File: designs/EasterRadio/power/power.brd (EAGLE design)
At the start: 31 x 44 mm, 23 parts, among them IC1 MCP73832T-2ACI_OT, IC2 TPS62160DGKR, IC3 DMP1045U-7, J1 10118192-0001LF, J2 S2B-PH-SM4

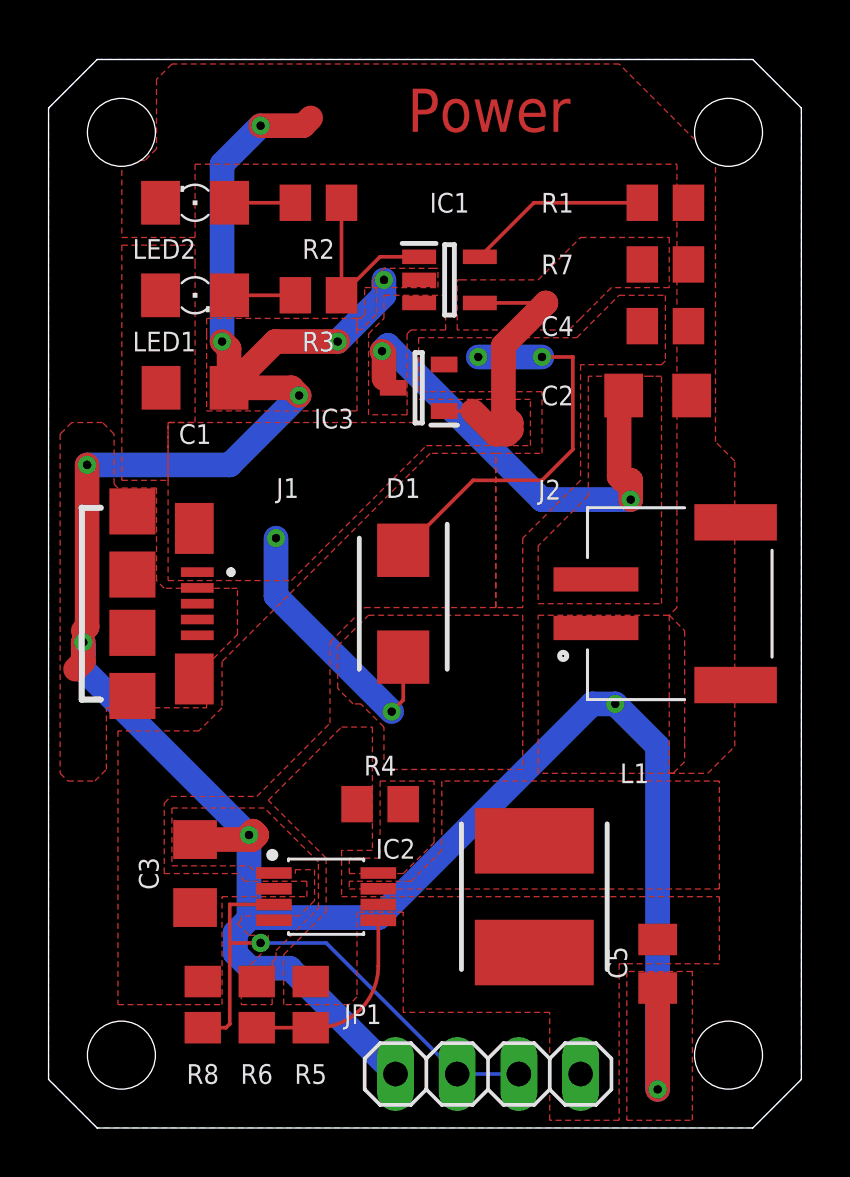
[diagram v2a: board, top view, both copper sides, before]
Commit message: added esd for rs232 to can
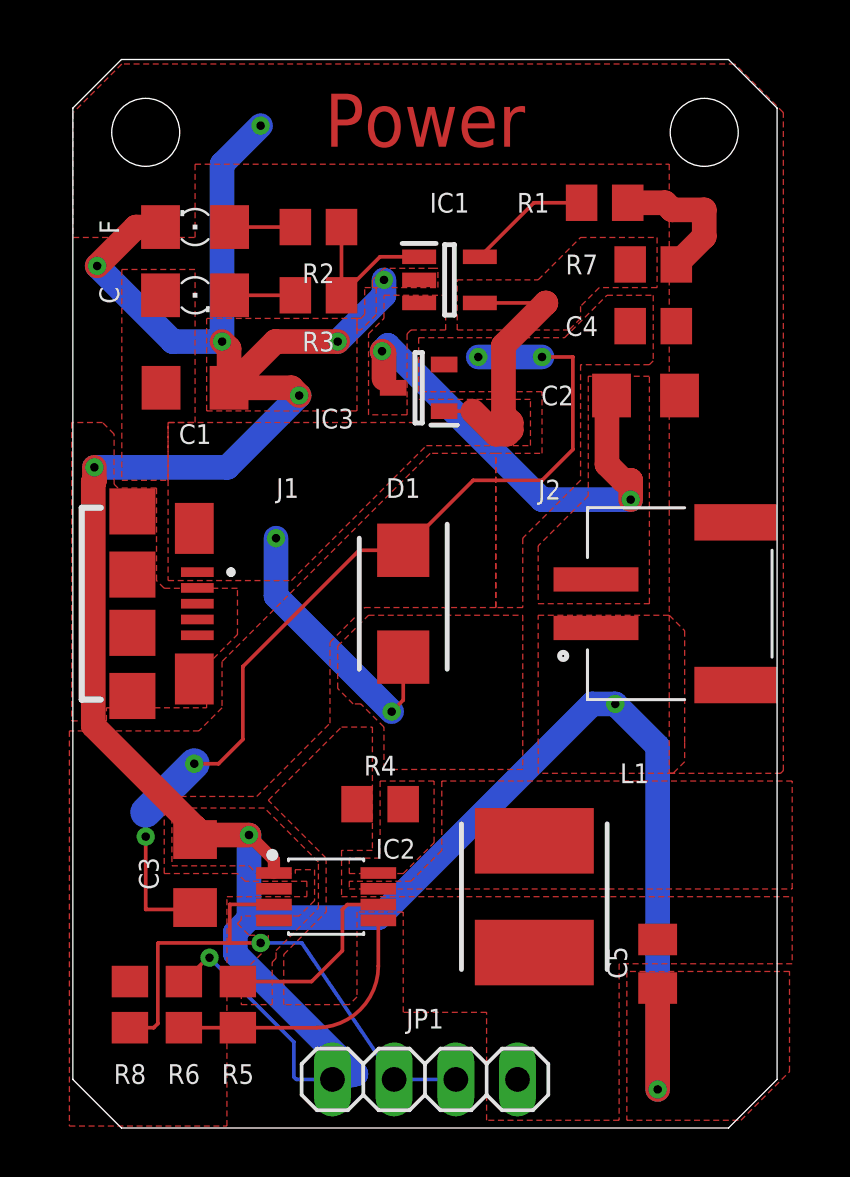
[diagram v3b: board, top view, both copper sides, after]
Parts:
- removed LED2: (no value), CommonParts:1206
- added F: (no value), CommonParts:1206
- moved R5 3.00 mm to (7.79, 5.08)
- moved R6 3.00 mm to (5.57, 5.08)
- moved R8 3.00 mm to (3.35, 5.08)
- moved JP1 2.61 mm to (15.5, 2.00)
- moved R1 2.50 mm to (22.9, 38.1)
- moved R2 1.00 mm to (11.1, 37.1)
- moved C2 0.50 mm to (24.6, 30.2)
- moved C4 0.50 mm to (24.9, 33.0)
- moved R7 0.50 mm to (24.9, 35.6)
- renumbered LED1 to C
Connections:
- net GNDA: now also F.C; no longer LED2.C
- net N$3: now also F.A; no longer LED2.A
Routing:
- net U_DRAIN: track 16.5 -> 39.4 mm, vias 2 -> 4
- net GNDA: track 110.5 -> 132.1 mm, vias 10 -> 11
- net 3.3V: track 0.00 -> 8.09 mm
- net FB: track 7.94 -> 10.9 mm
- net N$1: track 7.61 -> 5.11 mm
- net EN: track 22.1 -> 23.2 mm
- net STAT: track 7.66 -> 6.66 mm
- removed copper zone on layer 16, net GNDA
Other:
- board size 31 x 44 mm -> 29 x 44 mm

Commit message: added mainboard layout and new 3.5mm jack
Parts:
- added D2: LSM115JE3_TR13, CommonParts:DIOM5436X330N
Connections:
- net 5V: now also D2.1, JP1.2
- net EN: no longer JP1.2
- net GNDA: now also D2.2
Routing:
- net 5V: track 23.6 -> 60.7 mm, vias 2 -> 3
- net GNDA: track 132.1 -> 136.8 mm
- net EN: track 23.2 -> 25.0 mm, vias 1 -> 3
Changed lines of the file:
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@@
 <drawing>
 <settings>
-<setting alwaysvectorfont="yes"/>
+<setting alwaysvectorfont="no"/>
 <setting verticaltext="up"/>
 </settings>
-<grid distance="0.5" unitdist="mm" unit="mm" style="lines" multiple="1" display="yes" altdistance="5" altunitdist="mil" altunit="mil"/>
+<grid distance="0.1" unitdist="mm" unit="mm" style="lines" multiple="1" display="yes" altdistance="5" altunitdist="mil" altunit="mil"/>
 <layers>
 <layer number="1" name="Top" color="4" fill="1" visible="yes" active="yes"/>
@@
 <attribute name="VALUE" x="10.42" y="-1.175" size="1.27" layer="27"/>
 </element>
+<element name="D2" library="CommonParts" package="DIOM5436X330N" value="LSM115JE3_TR13" x="15.5" y="6" smashed="yes" rot="MR0">
+<attribute name="DESCRIPTION" value="Schottky Diodes &amp; Rectifiers Schottky" x="15.5" y="6" size="1.778" layer="28" rot="MR0" display="off"/>
+<attribute name="HEIGHT" value="3.3mm" x="15.5" y="6" size="1.778" layer="28" rot="MR0" display="off"/>
+<attribute name="MANUFACTURER_NAME" value="Microsemi Corporation" x="15.5" y="6" size="1.778" layer="28" rot="MR0" display="off"/>
+<attribute name="MANUFACTURER_PART_NUMBER" value="LSM115JE3/TR13" x="15.5" y="6" size="1.778" layer="28" rot="MR0" display="off"/>
+<attribute name="MOUSER_PART_NUMBER" value="494-LSM115JE3/TR13" x="15.5" y="6" size="1.778" layer="28" rot="MR0" display="off"/>
+<attribute name="MOUSER_PRICE-STOCK" value="https://www.mouser.com/Search/Refine.aspx?Keyword=494-LSM115JE3%2FTR13" x="15.5" y="6" size="1.778" layer="28" rot="MR0" display="off"/>
+<attribute name="NAME" x="10.5" y="6" size="0.8128" layer="26" rot="MR0" align="center"/>
+</element>
 </elements>
 <signals>
@@
 <contactref element="IC1" pad="2"/>
 <contactref element="J2" pad="1"/>
-<contactref element="J1" pad="5"/>
 <contactref element="C4" pad="2"/>
 <contactref element="F" pad="C"/>
@@
 <wire x1="9.2804" y1="11.0396" x2="8.255" y2="12.065" width="0.508" layer="1"/>
 <wire x1="5.5725" y1="6.03" x2="6.5557" y2="7.0132" width="0.1524" layer="1"/>
-<wire x1="6.5557" y1="7.0132" x2="6.62781875" y2="7.0132" width="0.1524" layer="1"/>
-<via x="6.62781875" y="7.0132" extent="1-16" drill="0.35"/>
-<wire x1="6.62781875" y1="7.0132" x2="10.1" y2="3.54101875" width="0.1524" layer="16"/>
-<wire x1="10.1" y1="3.54101875" x2="10.1" y2="2.1" width="0.1524" layer="16"/>
+<wire x1="6.5557" y1="7.0132" x2="6.72781875" y2="7.0132" width="0.1524" layer="1"/>
+<via x="6.72781875" y="7.0132" extent="1-16" drill="0.2"/>
+<wire x1="6.72781875" y1="7.0132" x2="10.1" y2="3.64101875" width="0.1524" layer="16"/>
+<wire x1="10.1" y1="3.64101875" x2="10.1" y2="2.1" width="0.1524" layer="16"/>
 <wire x1="10.1" y1="2.1" x2="10.2" y2="2" width="0.1524" layer="16"/>
 <wire x1="10.2" y1="2" x2="11.69" y2="2" width="0.1524" layer="16"/>
@@
 <wire x1="2" y1="35.5" x2="5.115" y2="32.385" width="1.016" layer="16"/>
 <wire x1="5.115" y1="32.385" x2="7.14375" y2="32.385" width="1.016" layer="16"/>
+<contactref element="J1" pad="5"/>
+<contactref element="D2" pad="2"/>
+<wire x1="11.69" y1="2" x2="11.69" y2="4.39" width="1.016" layer="16"/>
+<wire x1="11.69" y1="4.39" x2="13.3" y2="6" width="1.016" layer="16"/>
 </signal>
 <signal name="N$10">
@@
 <vertex x="25.05875" y="34.6075"/>
 <vertex x="22.6775" y="34.6075"/>
-<vertex x="21.9075" y="33.8375"/>
-<vertex x="21.9075" y="33.3375"/>
-<vertex x="21.43125" y="32.86125"/>
+<vertex x="20.93125" y="32.86125"/>
 <vertex x="16.8275" y="32.86125"/>
 </polygon>
@@
 </polygon>
 <wire x1="14.605" y1="19.39" x2="14.605" y2="17.62125" width="0.1524" layer="1"/>
-<wire x1="14.605" y1="17.62125" x2="14.12875" y2="17.145" width="0.1524" layer="1"/>
+<wire x1="14.605" y1="17.62125" x2="14.241875" y2="17.258125" width="0.1524" layer="1"/>
 <via x="14.12875" y="17.145" extent="1-16" drill="0.35"/>
+<wire x1="14.241875" y1="17.258125" x2="14.12875" y2="17.145" width="0.1524" layer="1"/>
 <wire x1="14.12875" y1="17.145" x2="9.36625" y2="21.9075" width="1.016" layer="16"/>
 <wire x1="9.36625" y1="21.9075" x2="9.36625" y2="24.28875" width="1.016" layer="16"/>
@@
 <wire x1="20.47875" y1="33.9725" x2="20.47625" y2="33.975" width="1.016" layer="1"/>
 <wire x1="20.47625" y1="33.975" x2="17.76" y2="33.975" width="0.1524" layer="1"/>
+<contactref element="D2" pad="1"/>
+<contactref element="JP1" pad="2"/>
+<wire x1="17.7" y1="6" x2="16.7" y2="5" width="1.016" layer="16"/>
+<wire x1="16.7" y1="5" x2="15.5" y2="5" width="1.016" layer="16"/>
+<wire x1="15.5" y1="5" x2="14.23" y2="3.73" width="1.016" layer="16"/>
+<wire x1="14.23" y1="3.73" x2="14.23" y2="2" width="1.016" layer="16"/>
+<wire x1="17.7" y1="6" x2="17" y2="6.7" width="1.016" layer="16"/>
+<wire x1="17" y1="6.7" x2="17" y2="9.5" width="1.016" layer="16"/>
+<wire x1="14.741875" y1="17.258125" x2="14.241875" y2="17.258125" width="1.016" layer="1"/>
+<wire x1="14.605" y1="19.39" x2="14.741875" y2="19.253125" width="1.016" layer="1"/>
+<wire x1="14.741875" y1="19.253125" x2="14.741875" y2="17.258125" width="1.016" layer="1"/>
+<wire x1="17" y1="9.5" x2="23.5" y2="9.5" width="1.016" layer="16"/>
+<wire x1="23.5" y1="9.5" x2="23.5" y2="15" width="1.016" layer="16"/>
+<wire x1="23.5" y1="15" x2="23" y2="15" width="1.016" layer="16"/>
+<via x="23" y="15" extent="1-16" drill="0.35"/>
+<wire x1="23" y1="15" x2="19.5" y2="15" width="1.016" layer="1"/>
+<wire x1="18" y1="16.5" x2="18" y2="19.5" width="1.016" layer="1"/>
+<wire x1="18" y1="19.5" x2="14.98875" y2="19.5" width="1.016" layer="1"/>
+<wire x1="14.98875" y1="19.5" x2="14.741875" y2="19.253125" width="1.016" layer="1"/>
+<wire x1="19.5" y1="15" x2="18" y2="16.5" width="1.016" layer="1"/>
 </signal>
 <signal name="U_DRAIN">
@@
 <contactref element="IC2" pad="3"/>
 <contactref element="R8" pad="2"/>
-<contactref element="JP1" pad="2"/>
 <contactref element="JP1" pad="3"/>
 <wire x1="7.46125" y1="7.62" x2="7.46125" y2="9.2075" width="0.1524" layer="1"/>
 <wire x1="7.46125" y1="9.2075" x2="9.2729" y2="9.2075" width="0.1524" layer="1"/>
 <wire x1="9.2729" y1="9.2075" x2="9.2804" y2="9.2" width="0.1524" layer="1"/>
-<wire x1="7.46125" y1="7.62" x2="8.7" y2="7.62" width="0.1524" layer="1"/>
+<wire x1="7.46125" y1="7.62" x2="8.73125" y2="7.62" width="0.1524" layer="1"/>
 <via x="8.73125" y="7.62" extent="1-16" drill="0.3556"/>
-<wire x1="8.7" y1="7.62" x2="8.73125" y2="7.62" width="0.1524" layer="1"/>
-<wire x1="8.73125" y1="7.62" x2="10.43" y2="7.62" width="0.1524" layer="16"/>
-<wire x1="10.43" y1="7.62" x2="14.23" y2="2" width="0.1524" layer="16"/>
-<wire x1="16.77" y1="2" x2="14.23" y2="2" width="0.1524" layer="16"/>
+<wire x1="10.43" y1="7.62" x2="8.73125" y2="7.62" width="0.1524" layer="16"/>
 <wire x1="3.35" y1="4.13" x2="4.33" y2="4.13" width="0.1524" layer="1"/>
 <wire x1="4.33" y1="4.13" x2="4.5" y2="4.3" width="0.1524" layer="1"/>
@@
 <wire x1="4.5" y1="7.6" x2="4.52" y2="7.62" width="0.1524" layer="1"/>
 <wire x1="4.52" y1="7.62" x2="7.46125" y2="7.62" width="0.1524" layer="1"/>
+<wire x1="16.77" y1="2" x2="15.5" y2="3.27" width="0.1524" layer="16"/>
+<wire x1="15.5" y1="3.27" x2="15.5" y2="3.5" width="0.1524" layer="16"/>
+<via x="15.5" y="3.5" extent="1-16" drill="0.35"/>
+<wire x1="15.5" y1="3.5" x2="15.5" y2="7.5" width="0.1524" layer="1"/>
+<via x="15.5" y="7.5" extent="1-16" drill="0.35"/>
+<wire x1="15.5" y1="7.5" x2="10.55" y2="7.5" width="0.1524" layer="16"/>
+<wire x1="10.55" y1="7.5" x2="10.43" y2="7.62" width="0.1524" layer="16"/>
 </signal>
 </signals>

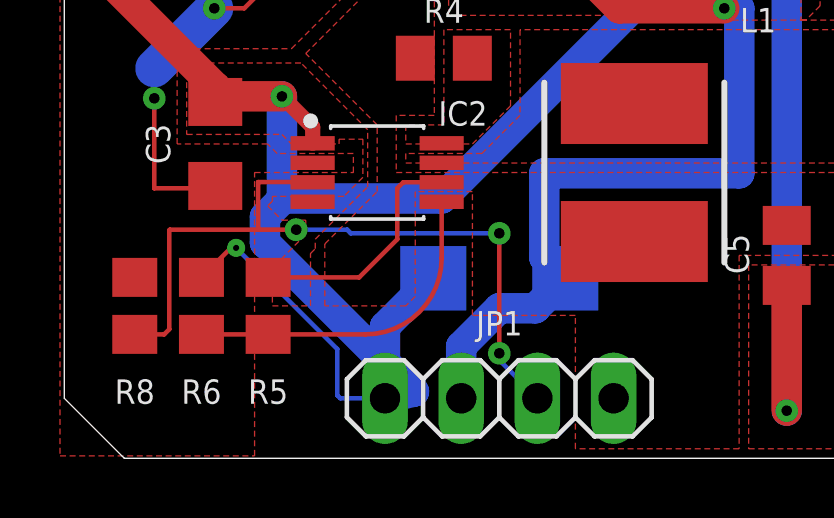
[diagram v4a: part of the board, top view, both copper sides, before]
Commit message: added more stuff to pcb main for radio
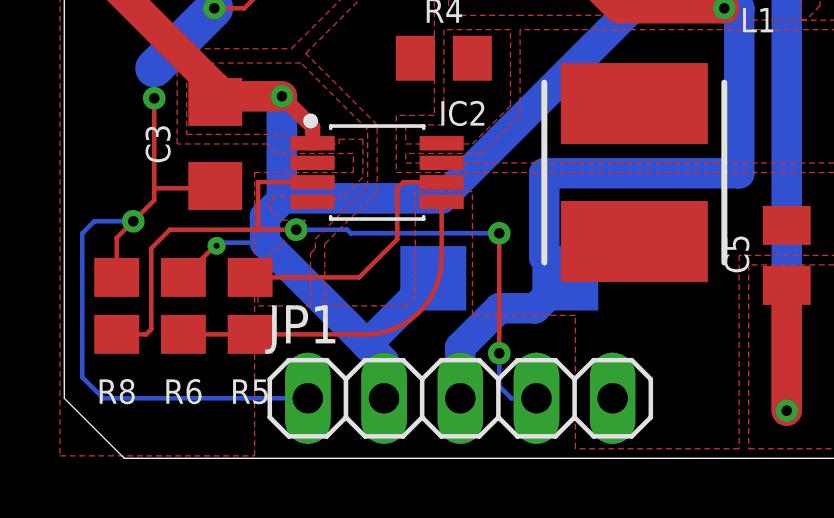
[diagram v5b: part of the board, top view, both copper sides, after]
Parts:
- JP1: device pinhead:1X04 -> pinhead:1X05
- moved JP1 1.30 mm to (14.2, 2.00)
- moved R8 0.60 mm to (2.75, 5.08)
- moved R5 0.60 mm to (7.20, 5.08)
- moved R6 0.60 mm to (4.97, 5.08)
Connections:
- net 3.3V: now also JP1.5; no longer JP1.4
- net 5V: now also JP1.3; no longer JP1.2
- net EN: now also JP1.4; no longer JP1.3
- net GNDA: now also JP1.2; no longer JP1.1
- net U_DRAIN: now also JP1.1
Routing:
- net U_DRAIN: track 39.4 -> 57.4 mm, vias 4 -> 5
- net GNDA: track 136.8 -> 127.9 mm
- net EN: track 25.0 -> 26.0 mm
- net FB: track 10.9 -> 11.5 mm
- net 3.3V: track 8.09 -> 8.69 mm

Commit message: started board routing
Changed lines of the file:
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@@
 <setting verticaltext="up"/>
 </settings>
-<grid distance="0.01" unitdist="mm" unit="mm" style="lines" multiple="1" display="yes" altdistance="5" altunitdist="mil" altunit="mil"/>
+<grid distance="0.1" unitdist="mm" unit="mm" style="lines" multiple="1" display="yes" altdistance="5" altunitdist="mil" altunit="mil"/>
 <layers>
 <layer number="1" name="Top" color="4" fill="1" visible="yes" active="yes"/>
@@
 </element>
 <element name="R5" library="CommonParts" package="R0805" package3d_urn="urn:adsk.eagle:package:23553/2" value="68kOhm" x="7.195" y="5.08" smashed="yes" rot="R90">
-<attribute name="NAME" x="7.195" y="2.2225" size="0.8128" layer="25" rot="R180" align="center"/>
+<attribute name="NAME" x="6.595" y="2.2225" size="0.8128" layer="25" rot="R180" align="center"/>
 </element>
 <element name="R6" library="CommonParts" package="R0805" package3d_urn="urn:adsk.eagle:package:23553/2" value="22kOhm" x="4.9725" y="5.08" smashed="yes" rot="R270">
-<attribute name="NAME" x="4.9725" y="2.2225" size="0.8128" layer="25" align="center"/>
+<attribute name="NAME" x="4.3725" y="2.2225" size="0.8128" layer="25" align="center"/>
 </element>
 <element name="R3" library="CommonParts" package="R0805" package3d_urn="urn:adsk.eagle:package:23553/2" value="470ohm" x="11.1125" y="34.29" smashed="yes">
@@
 </element>
 <element name="R8" library="CommonParts" package="R0805" package3d_urn="urn:adsk.eagle:package:23553/2" value="10kOhm" x="2.75" y="5.08" smashed="yes" rot="R270">
-<attribute name="NAME" x="2.75" y="2.2225" size="0.8128" layer="25" align="center"/>
+<attribute name="NAME" x="2.15" y="2.2225" size="0.8128" layer="25" align="center"/>
 </element>
 <element name="D2" library="CommonParts" package="DIOM5436X330N" value="LSM115JE3_TR13" x="15.5" y="6" smashed="yes" rot="MR0">
@@
 </element>
 <element name="JP1" library="pinhead" library_urn="urn:adsk.eagle:library:325" package="1X05" package3d_urn="urn:adsk.eagle:package:22469/2" value="" x="14.2" y="2" smashed="yes">
-<attribute name="NAME" x="7.7738" y="3.8288" size="1.27" layer="25" ratio="10"/>
+<attribute name="NAME" x="19.7638" y="4.0588" size="1.27" layer="25" ratio="10"/>
 <attribute name="POPULARITY" value="69" x="14.2" y="2" size="1.778" layer="27" display="off"/>
 <attribute name="VALUE" x="7.85" y="-1.175" size="1.27" layer="27"/>
@@
 <vertex x="8.255" y="7.9375"/>
 <vertex x="9.04875" y="7.9375"/>
-<vertex x="7.46125" y="6.35"/>
-<vertex x="7.46125" y="5.08"/>
+<vertex x="7.68125" y="6.57"/>
+<vertex x="7.68125" y="5.08"/>
 <vertex x="9.2075" y="5.08"/>
 <vertex x="9.2075" y="6.82625"/>

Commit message: changed poti and encoder pcb to correct schematic and brd + mainboard change for push btn on rotary encoder
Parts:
- R5: value 68kOhm -> 562kOhm
- R6: value 22kOhm -> 180kOhm
- R8: value 10kOhm -> 200kOhm
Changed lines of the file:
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@@
 </layers>
 <board>
-<fusionsync huburn="a.cGVyc29uYWw6dWUyYTNmMDU1" projecturn="a.cGVyc29uYWw6dWUyYTNmMDU1IzIwMTgxMjEwMTY0OTQ5MjI2" f3durn="urn:adsk.wipprod:dm.lineage:3cznDv7KT36rVomoCqRWPA" pcbguid="" lastpulledtime="" lastsyncedchangeguid="" latestrevisionid="2dbd548e-a3dd-49c0-bbff-32b45b5b9153" lastsyncedrevisionid="2dbd548e-a3dd-49c0-bbff-32b45b5b9153" lastboardhashguid="febd1a38-2622-4c81-96de-2d81002e64d9" lastpushedtime="2020-12-07T17:29:31Z" linktopcb3d="true"/>
+<fusionsync huburn="a.cGVyc29uYWw6dWUyYTNmMDU1" projecturn="a.cGVyc29uYWw6dWUyYTNmMDU1IzIwMTgxMjEwMTY0OTQ5MjI2" f3durn="urn:adsk.wipprod:dm.lineage:3cznDv7KT36rVomoCqRWPA" pcbguid="" lastpulledtime="" lastsyncedchangeguid="" latestrevisionid="2dbd548e-a3dd-49c0-bbff-32b45b5b9153" lastsyncedrevisionid="2dbd548e-a3dd-49c0-bbff-32b45b5b9153" lastboardhashguid="febd1a38-2622-4c81-96de-2d81002e64d9" lastpushedtime="2020-12-07T17:29:31Z" linktopcb3d="false"/>
 <plain>
 <text x="15.5" y="41.5" size="2.1844" layer="29" font="vector" ratio="15" align="center">Power</text>
@@
 <attribute name="NAME" x="13.6525" y="14.9225" size="0.8128" layer="25" rot="R180" align="center"/>
 </element>
-<element name="R5" library="CommonParts" package="R0805" package3d_urn="urn:adsk.eagle:package:23553/2" value="68kOhm" x="7.195" y="5.08" smashed="yes" rot="R90">
+<element name="R5" library="CommonParts" package="R0805" package3d_urn="urn:adsk.eagle:package:23553/2" value="562kOhm" x="7.195" y="5.08" smashed="yes" rot="R90">
 <attribute name="NAME" x="6.595" y="2.2225" size="0.8128" layer="25" rot="R180" align="center"/>
 </element>
-<element name="R6" library="CommonParts" package="R0805" package3d_urn="urn:adsk.eagle:package:23553/2" value="22kOhm" x="4.9725" y="5.08" smashed="yes" rot="R270">
+<element name="R6" library="CommonParts" package="R0805" package3d_urn="urn:adsk.eagle:package:23553/2" value="180kOhm" x="4.9725" y="5.08" smashed="yes" rot="R270">
 <attribute name="NAME" x="4.3725" y="2.2225" size="0.8128" layer="25" align="center"/>
 </element>
@@
 <attribute name="NAME" x="21.955" y="35.56" size="0.8128" layer="25" rot="R180" align="center"/>
 </element>
-<element name="R8" library="CommonParts" package="R0805" package3d_urn="urn:adsk.eagle:package:23553/2" value="10kOhm" x="2.75" y="5.08" smashed="yes" rot="R270">
+<element name="R8" library="CommonParts" package="R0805" package3d_urn="urn:adsk.eagle:package:23553/2" value="200kOhm" x="2.75" y="5.08" smashed="yes" rot="R270">
 <attribute name="NAME" x="2.15" y="2.2225" size="0.8128" layer="25" align="center"/>
 </element>
